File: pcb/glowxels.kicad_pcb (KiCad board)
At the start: 2 copper layers, 97.3 x 25 mm, 84 parts, among them J1 OUT, J2 IN, U1 STP16CPC26, U2 STP16CPC26, U3 STP16CPC26, U4 STP16CPC26

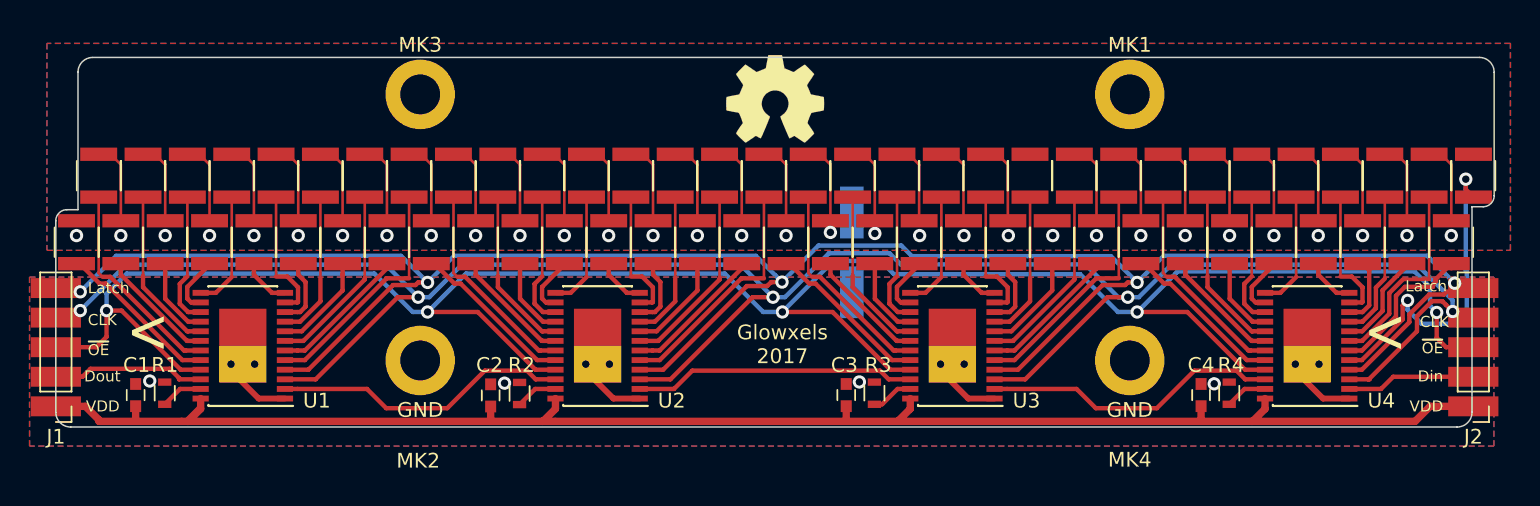
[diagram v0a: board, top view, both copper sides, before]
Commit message: rename glowxels/ -> pcb/. Smallish tweak in PCB.
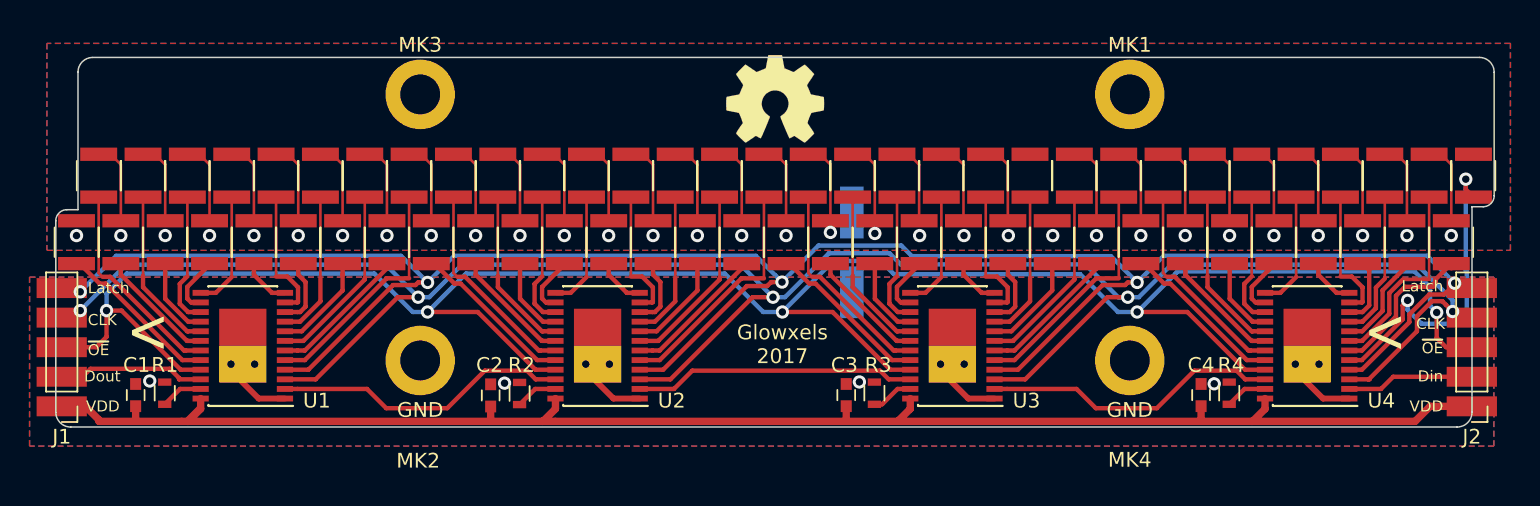
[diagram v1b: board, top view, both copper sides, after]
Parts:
- moved J1 0.40 mm to (99.0, 111.1)
- moved J2 0.10 mm to (194.4, 111.1)
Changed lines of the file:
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@@
   )
   (setup
-    (last_trace_width 0.3)
+    (last_trace_width 0.18)
     (user_trace_width 0.2)
     (user_trace_width 0.25)
@@
   )
   (module Pin_Headers:Pin_Header_Straight_1x05_Pitch2.00mm (layer F.Cu)
-    (at 194.488 111.102 180)
+    (at 194.388 111.102 180)
     (descr "Through hole straight pin header, 1x05, 2.00mm pitch, single row")
     (tags "Through hole pin header THT 1x05 2.00mm single row")
@@
   )
   (module Pin_Headers:Pin_Header_Straight_1x05_Pitch2.00mm (layer F.Cu)
-    (at 98.603 111.102 180)
+    (at 99 111.102 180)
     (descr "Through hole straight pin header, 1x05, 2.00mm pitch, single row")
     (tags "Through hole pin header THT 1x05 2.00mm single row")
@@
     (effects (font (size 0.75 0.75) (thickness 0.15)) (justify right))
   )
-  (gr_text Latch (at 192.71 102.974) (layer F.SilkS)
+  (gr_text Latch (at 192.456 102.974) (layer F.SilkS)
     (effects (font (size 0.75 0.75) (thickness 0.15)) (justify right))
   )
@@
     (effects (font (size 0.75 0.75) (thickness 0.15)) (justify right))
   )
-  (gr_text CLK (at 192.837 105.387) (layer F.SilkS)
+  (gr_text CLK (at 192.583 105.514) (layer F.SilkS)
     (effects (font (size 0.75 0.75) (thickness 0.15)) (justify right))
   )

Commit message: Update to work with schematic and footprint library of 5.1
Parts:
- C1, C2, C3, C4: footprint Capacitors_SMD:C_0603 -> Capacitor_SMD:C_0603_1608Metric
- C5: footprint Capacitors_SMD:CP_Elec_6.3x5.3 -> Capacitor_SMD:CP_Elec_6.3x5.3
- D1, D10, D11, D12, D13, D14, D15, D16, D17, D18, D19, D2, D20, D21, D22, D23, D24, D25, D26, D27, D28, D29, D3, D30, D31, D32, D33, D34, D35, D36, D37, D38, D39, D4, D40, D41, D42, D43, D44, D45, D46, D47, D48, D49, D5, D50, D51, D52, D53, D54, D55, D56, D57, D58, D59, D6, D60, D61, D62, D63, D64, D7, D8, D9: footprint Resistors_SMD:R_1210 -> Glowxels:LED_1210
- J1, J2: footprint Pin_Headers:Pin_Header_Straight_1x05_Pitch2.00mm -> Glowxels:EdgeConnect
- R1, R2, R3, R4: footprint Resistors_SMD:R_0603 -> Resistor_SMD:R_0603_1608Metric
- moved R1 0.13 mm to (106.0, 110.3)
- moved R3 0.13 mm to (154.0, 110.3)
- moved R4 0.13 mm to (178.0, 110.3)
- moved R2 0.11 mm to (130.0, 110.3)

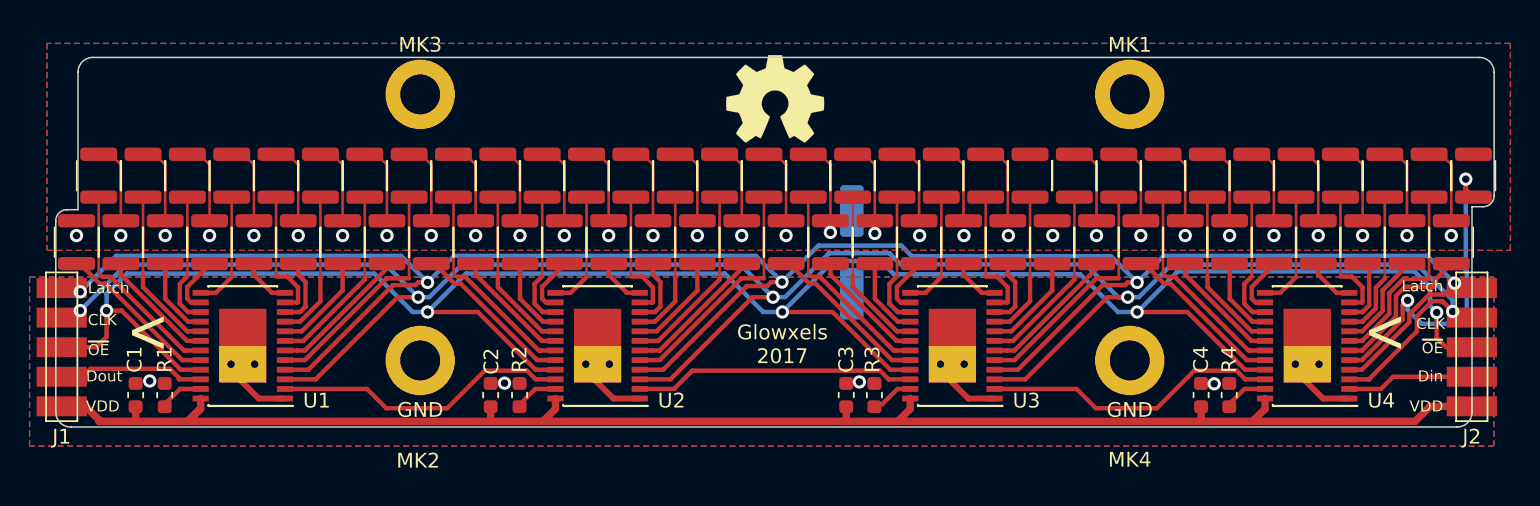
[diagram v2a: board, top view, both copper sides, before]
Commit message: Add inner edge fillet; connect LED power plane with thermal reliefs.
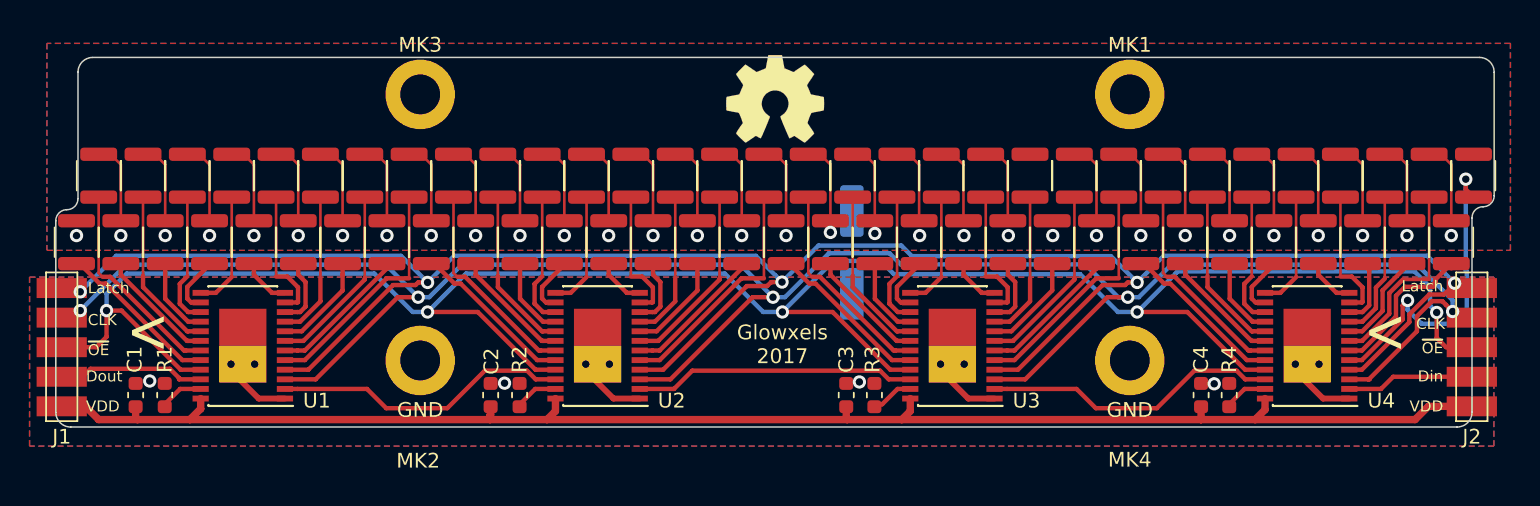
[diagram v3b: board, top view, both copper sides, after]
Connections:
- net Net-(D1-Pad1) renamed /FirstLed
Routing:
- net /VDD: track 110.9 -> 107.5 mm
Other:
- outline, holes or cut-outs redrawn

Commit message: Adapt to Kicad 6
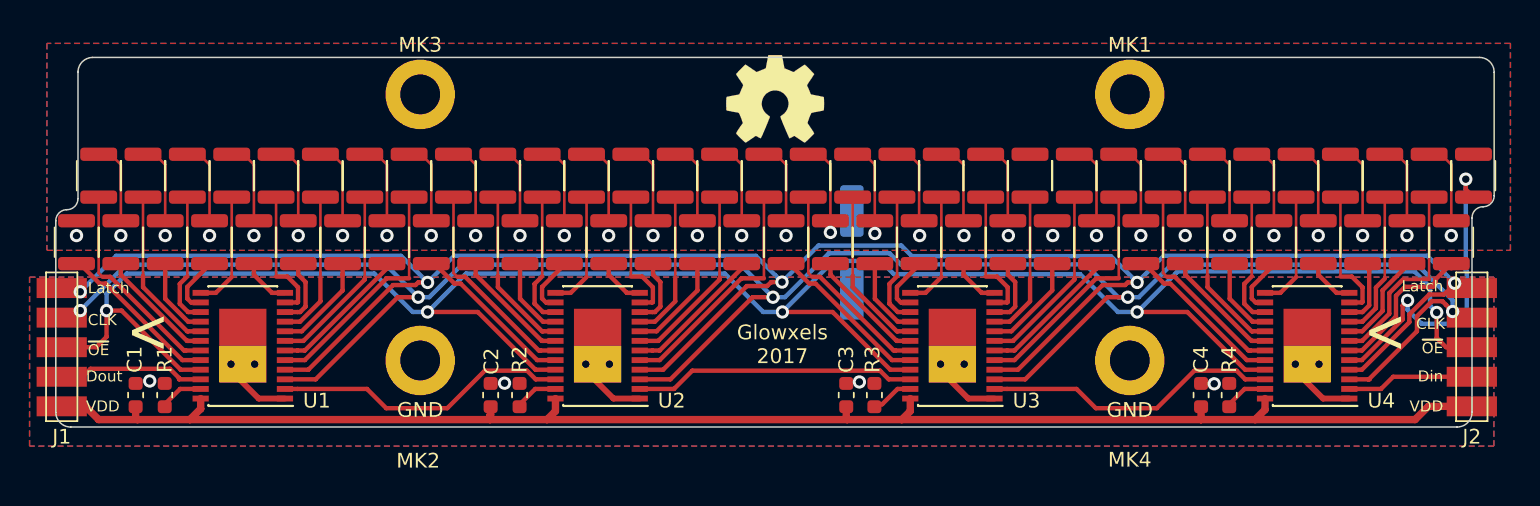
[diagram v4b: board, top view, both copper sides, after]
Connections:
- net /~OE renamed /~{OE}
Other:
- net class Default removed
- board text added: "~{OE}"
- board text removed: "~OE"
